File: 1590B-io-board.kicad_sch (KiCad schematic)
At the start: 4 parts, among them J1 ACJS-MHOM, J2 ACJS-MHOM, J3 Conn_01x04

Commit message: Add a few misc. adjustments
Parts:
- added D1: LED, LED_THT:LED_D3.0mm, symbol Device:LED
- added R1: R, Resistor_THT:R_Axial_DIN0204_L3.6mm_D1.6mm_P5.08mm_Horizontal, symbol Device:R
- J3: footprint 1590:01x06_1.27mm_Ribbon_Pads -> 1590:01x06_2.54mm_Ribbon_Pads
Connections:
- net 9V: now also J3.6 (Pin_6), R1.2; no longer J3.3 (Pin_3), S1.4
- net FX_INPUT: now also J3.3 (Pin_3); no longer J3.2 (Pin_2)
- net FX_OUTPUT: now also J3.4 (Pin_4); no longer J3.5 (Pin_5)
- net GND: now also J3.5 (Pin_5); no longer J3.6 (Pin_6)
- net OUTPUT_JACK_TIP: now also J3.2 (Pin_2); no longer J3.4 (Pin_4)
- new net: D1.2 (A), R1.1
- new net: D1.1 (K), S1.4
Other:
- company: (none) -> Silicon-based LIfeforms
- title: (none) -> 1590B I/O Board
- moved on the sheet: J1, J2, J3, S1

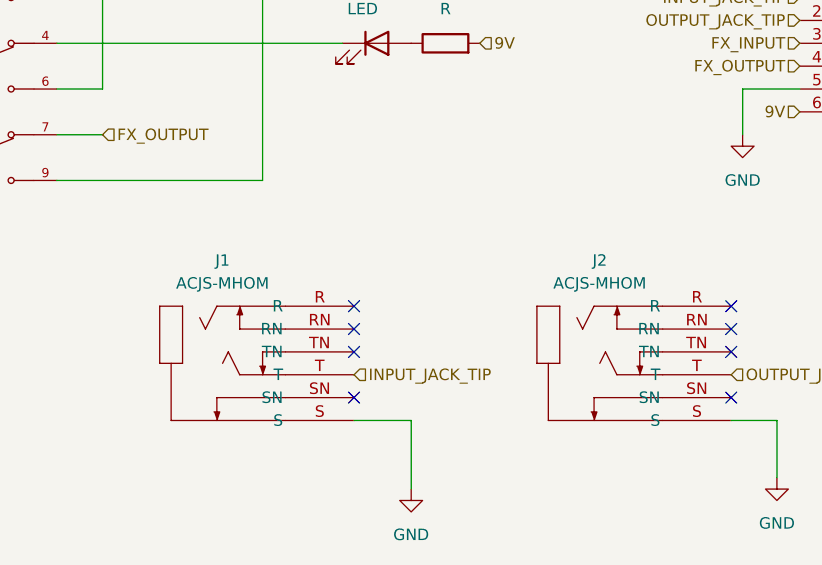
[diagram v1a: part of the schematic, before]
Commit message: Update board dimensions and jack layout
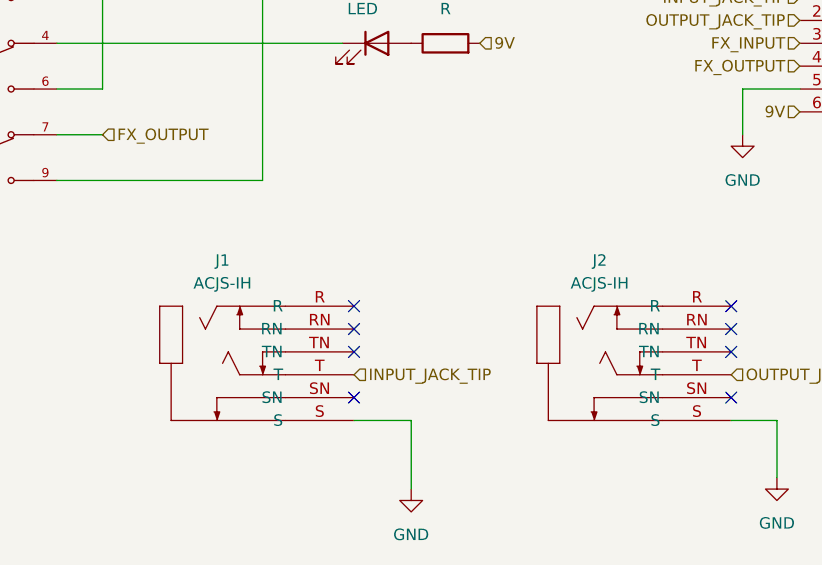
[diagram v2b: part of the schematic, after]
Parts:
- J1, J2: value ACJS-MHOM -> ACJS-IH; footprint 1590:Amphenol_ACJS-IH -> KicadAudio:Amphenol_ACJS-IH; symbol ACJS-IH:ACJS-IH -> KiCadAudio:ACJS-IH
- R1: footprint Resistor_THT:R_Axial_DIN0204_L3.6mm_D1.6mm_P5.08mm_Horizontal -> Resistor_THT:R_Axial_DIN0207_L6.3mm_D2.5mm_P7.62mm_Horizontal
- S1: footprint 1590:Tayda_3PDT_A-1844 -> Pedals:Tayda_3PDT; symbol 3PDT:3PDT -> KiCadAudio:3PDT
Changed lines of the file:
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@@
 			)
 		)
-		(property "Footprint" "Resistor_THT:R_Axial_DIN0204_L3.6mm_D1.6mm_P5.08mm_Horizontal"
+		(property "Footprint" "Resistor_THT:R_Axial_DIN0207_L6.3mm_D2.5mm_P7.62mm_Horizontal"
 			(at 149.86 81.788 90)
 			(effects
@@
 	)
 	(symbol
-		(lib_id "3PDT:3PDT")
+		(lib_id "KiCadAudio:3PDT")
 		(at 99.06 82.55 0)
 		(unit 1)
@@
 			)
 		)
-		(property "Footprint" "1590:Tayda_3PDT_A-1844"
+		(property "Footprint" "Pedals:Tayda_3PDT"
 			(at 99.06 82.55 0)
 			(effects
@@
 	)
 	(symbol
-		(lib_id "ACJS-IH:ACJS-IH")
+		(lib_id "KiCadAudio:ACJS-IH")
 		(at 181.61 109.22 0)
 		(unit 1)
@@
 			)
 		)
-		(property "Value" "ACJS-MHOM"
+		(property "Value" "ACJS-IH"
 			(at 167.005 106.68 0)
 			(effects
@@
 			)
 		)
-		(property "Footprint" "1590:Amphenol_ACJS-IH"
+		(property "Footprint" "KicadAudio:Amphenol_ACJS-IH"
 			(at 181.61 109.22 0)
 			(effects
@@
 	)
 	(symbol
-		(lib_id "ACJS-IH:ACJS-IH")
+		(lib_id "KiCadAudio:ACJS-IH")
 		(at 139.7 109.22 0)
 		(unit 1)
@@
 			)
 		)
-		(property "Value" "ACJS-MHOM"
+		(property "Value" "ACJS-IH"
 			(at 125.095 106.68 0)
 			(effects
@@
 			)
 		)
-		(property "Footprint" "1590:Amphenol_ACJS-IH"
+		(property "Footprint" "KicadAudio:Amphenol_ACJS-IH"
 			(at 139.7 109.22 0)
 			(effects
